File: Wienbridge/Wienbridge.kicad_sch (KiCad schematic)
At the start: 23 parts, among them J1 OUTPUT, U1 OP07, U2 OP07, U3 OP07

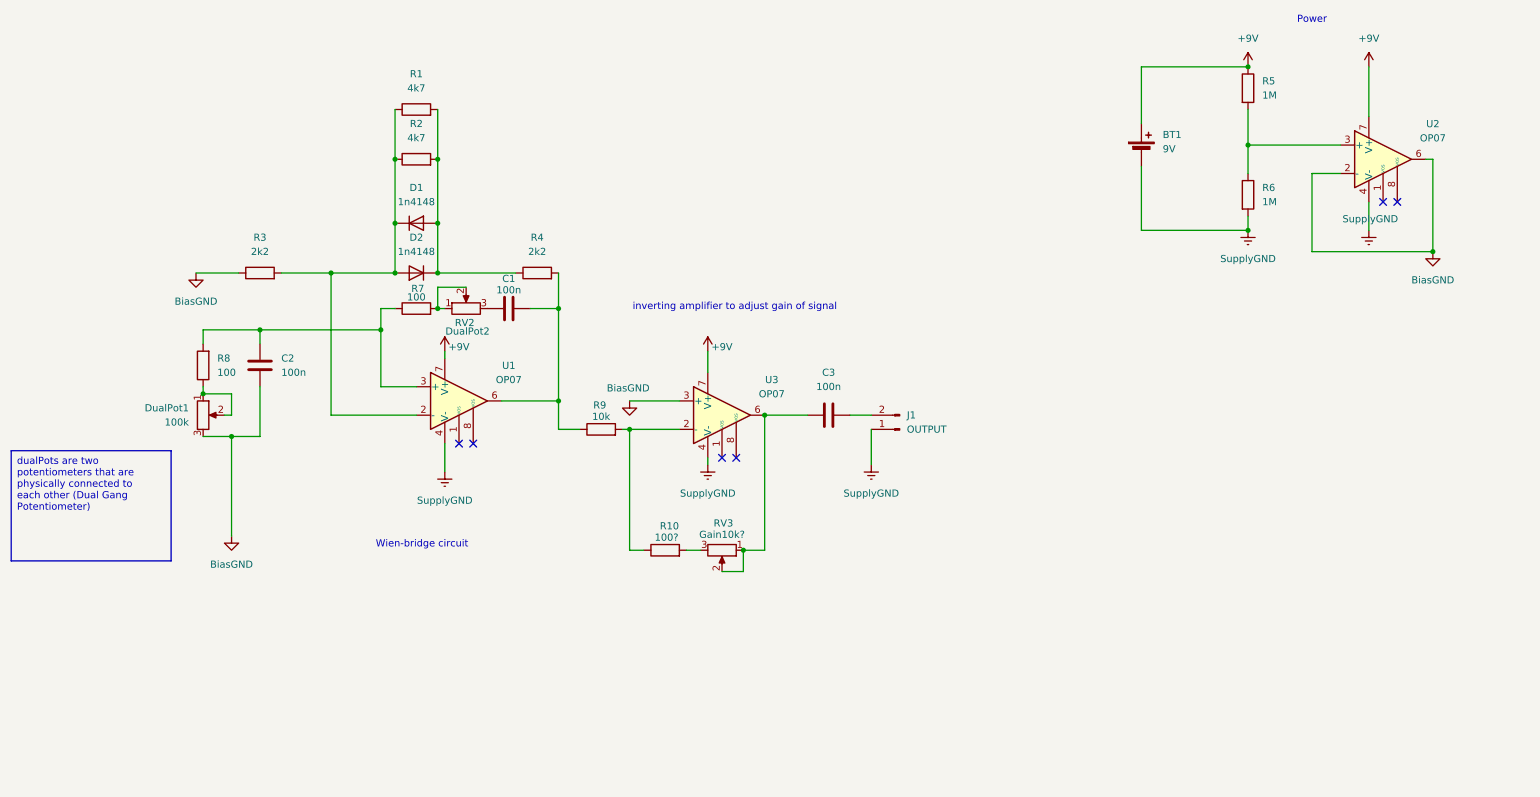
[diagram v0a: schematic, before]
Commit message: finished first revision of the pcb of wien-bridge
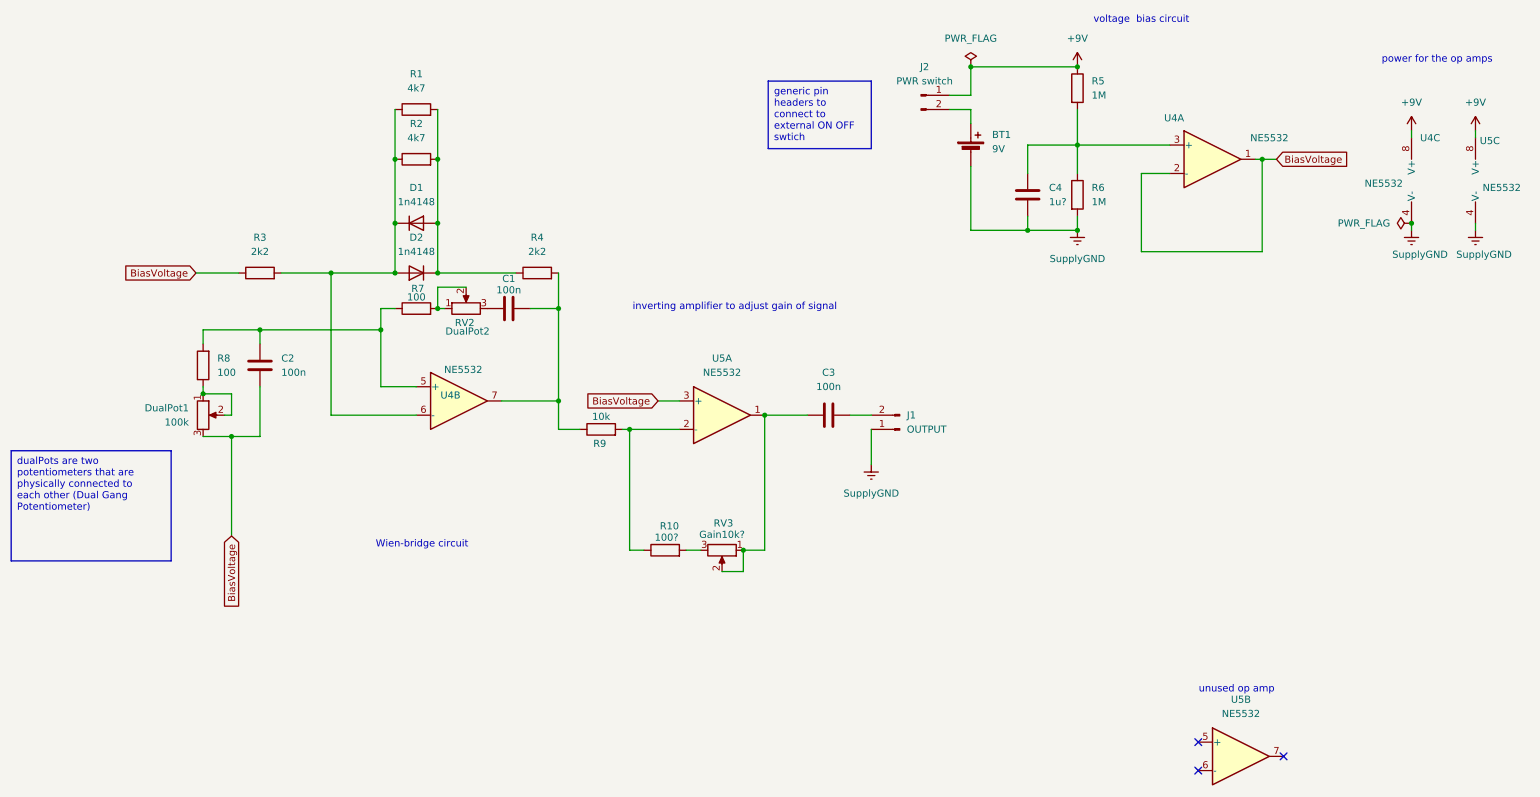
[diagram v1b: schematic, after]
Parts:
- removed U1, U2, U3: OP07, symbol Amplifier_Operational:OP07
- added C4: 1u?, Capacitor_SMD:C_0603_1608Metric_Pad1.08x0.95mm_HandSolder, symbol Device:C
- added J2: PWR switch, Connector_PinHeader_2.54mm:PinHeader_1x02_P2.54mm_Vertical, symbol Connector:Conn_01x02_Pin
- added U4, U5: NE5532, Package_DIP:DIP-8_W7.62mm, symbol Amplifier_Operational:NE5532
- R10: footprint (none) -> Resistor_SMD:R_0603_1608Metric_Pad0.98x0.95mm_HandSolder
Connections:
- net +9V: now also J2.1 (Pin_1), U4.8 (V+), U5.8 (V+); no longer BT1.1 (+)
- net SupplyGND: now also C4.2, U4.4 (V-), U5.4 (V-)
- net at D1.1 (K), D2.2 (A), R1.1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: now also U4.6 (-)
- net at C1.2, R4.2, R9.1: now also U4.7
- net at R10.1, R9.2: now also U5.2 (-)
- net at C2.1, R7.1, R8.2: now also U4.5 (+)
- net at C3.1, RV3.1, RV3.2: now also U5.1
- net at R5.2, R6.1: now also C4.1, U4.3 (+)
- net BiasGND renamed BiasVoltage
- net BiasVoltage: now also U4.1, U4.2 (-), U5.3 (+)
- new net: BT1.1 (+), J2.2 (Pin_2)
- no-connect marks 6 -> 3
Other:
- note added: "power for the op amps"
- note added: "unused op amp"
- note added: "voltage bias circuit"
- note removed: "Power"
- moved on the sheet: BT1, R5, R6

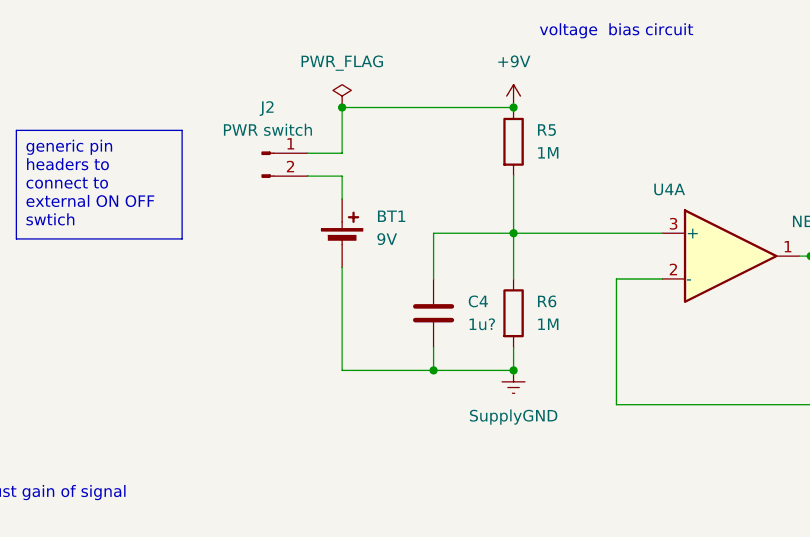
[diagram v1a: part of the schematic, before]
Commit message: few additions to the wein-brdige circuit and finished first revision of the opamp distortion schematic
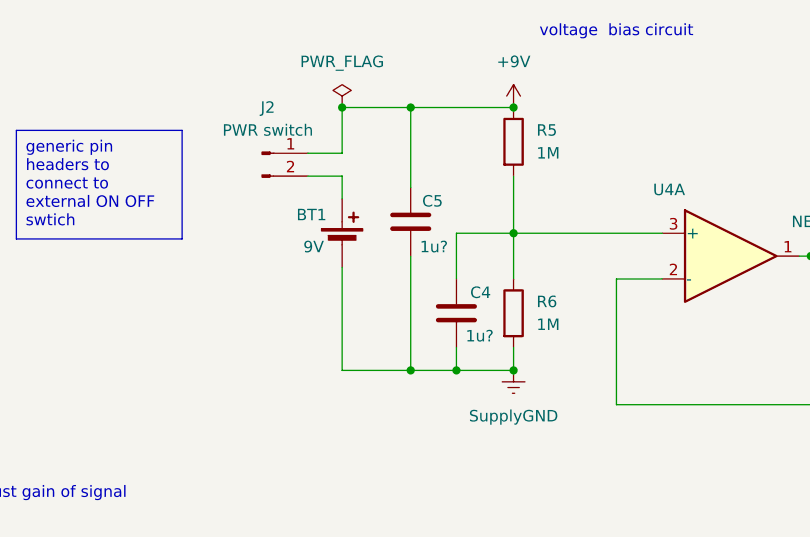
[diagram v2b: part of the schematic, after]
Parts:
- added C5: 1u?, Capacitor_SMD:C_0603_1608Metric_Pad1.08x0.95mm_HandSolder, symbol Device:C
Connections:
- net +9V: now also C5.1
- net SupplyGND: now also C5.2
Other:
- moved on the sheet: C4
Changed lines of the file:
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@@
 	)
 	(junction
+		(at 196.85 54.61)
+		(diameter 0)
+		(color 0 0 0 0)
+	)
+	(junction
 		(at 110.49 68.58)
 		(diameter 0)
@@
 	)
 	(junction
+		(at 191.77 25.4)
+		(diameter 0)
+		(color 0 0 0 0)
+	)
+	(junction
+		(at 191.77 54.61)
+		(diameter 0)
+		(color 0 0 0 0)
+	)
+	(junction
 		(at 81.28 41.91)
 		(diameter 0)
@@
 	)
 	(junction
-		(at 194.31 54.61)
-		(diameter 0)
-		(color 0 0 0 0)
-	)
-	(junction
 		(at 46.99 83.82)
 		(diameter 0)
@@
 	(wire
 		(pts
-			(xy 194.31 52.07) (xy 194.31 54.61)
+			(xy 196.85 52.07) (xy 196.85 54.61)
 		)
 		(stroke
@@
 	(wire
 		(pts
-			(xy 194.31 54.61) (xy 203.2 54.61)
-		)
-		(stroke
-			(width 0)
-			(type default)
-		)
-	)
-	(wire
-		(pts
 			(xy 214.63 58.42) (xy 236.22 58.42)
 		)
@@
 	(wire
 		(pts
-			(xy 194.31 39.37) (xy 203.2 39.37)
+			(xy 196.85 39.37) (xy 203.2 39.37)
 		)
 		(stroke
@@
 	(wire
 		(pts
+			(xy 196.85 54.61) (xy 203.2 54.61)
+		)
+		(stroke
+			(width 0)
+			(type default)
+		)
+	)
+	(wire
+		(pts
 			(xy 128.27 85.09) (xy 132.08 85.09)
 		)
@@
 	(wire
 		(pts
+			(xy 191.77 25.4) (xy 191.77 34.29)
+		)
+		(stroke
+			(width 0)
+			(type default)
+		)
+	)
+	(wire
+		(pts
 			(xy 147.32 87.63) (xy 154.94 87.63)
 		)
@@
 	(wire
 		(pts
+			(xy 191.77 54.61) (xy 196.85 54.61)
+		)
+		(stroke
+			(width 0)
+			(type default)
+		)
+	)
+	(wire
+		(pts
 			(xy 45.72 62.23) (xy 53.34 62.23)
 		)
@@
 	(wire
 		(pts
+			(xy 191.77 25.4) (xy 203.2 25.4)
+		)
+		(stroke
+			(width 0)
+			(type default)
+		)
+	)
+	(wire
+		(pts
 			(xy 139.7 115.57) (xy 143.51 115.57)
 		)
@@
 	(wire
 		(pts
-			(xy 184.15 25.4) (xy 203.2 25.4)
+			(xy 184.15 25.4) (xy 191.77 25.4)
 		)
 		(stroke
@@
 	(wire
 		(pts
-			(xy 184.15 54.61) (xy 194.31 54.61)
+			(xy 184.15 54.61) (xy 191.77 54.61)
 		)
 		(stroke
@@
 	(wire
 		(pts
-			(xy 194.31 44.45) (xy 194.31 39.37)
+			(xy 196.85 44.45) (xy 196.85 39.37)
 		)
 		(stroke
@@
 	(wire
 		(pts
+			(xy 191.77 41.91) (xy 191.77 54.61)
+		)
+		(stroke
+			(width 0)
+			(type default)
+		)
+	)
+	(wire
+		(pts
 			(xy 88.9 62.23) (xy 102.87 62.23)
 		)
@@
 		(on_board yes)
 		(dnp no)
-		(fields_autoplaced yes)
 		(property "Reference" "BT1"
-			(at 187.96 37.5284 0)
+			(at 179.07 37.338 0)
 			(effects
 				(font
@@
 		)
 		(property "Value" "9V"
-			(at 187.96 40.0684 0)
+			(at 179.832 40.894 0)
 			(effects
 				(font
@@
 	)
 	(symbol
+		(lib_id "Device:C")
+		(at 191.77 38.1 0)
+		(unit 1)
+		(exclude_from_sim no)
+		(in_bom yes)
+		(on_board yes)
+		(dnp no)
+		(property "Reference" "C5"
+			(at 193.04 35.814 0)
+			(effects
+				(font
+					(size 1.27 1.27)
+				)
+				(justify left)
+			)
+		)
+		(property "Value" "1u?"
+			(at 192.786 40.894 0)
+			(effects
+				(font
+					(size 1.27 1.27)
+				)
+				(justify left)
+			)
+		)
+		(property "Footprint" "Capacitor_SMD:C_0603_1608Metric_Pad1.08x0.95mm_HandSolder"
+			(at 192.7352 41.91 0)
+			(effects
+				(font
+					(size 1.27 1.27)
+				)
+				(hide yes)
+			)
+		)
+		(property "Datasheet" "~"
+			(at 191.77 38.1 0)
+			(effects
+				(font
+					(size 1.27 1.27)
+				)
+				(hide yes)
+			)
+		)
+		(property "Description" "Unpolarized capacitor"
+			(at 191.77 38.1 0)
+			(effects
+				(font
+					(size 1.27 1.27)
+				)
+				(hide yes)
+			)
+		)
+		(pin "2"
+		)
+		(pin "1"
+		)
+		(instances
+			(project ""
+				(path "/15d9c779-f062-42d2-9e52-f5c6a501706f"
+					(reference "C5")
+					(unit 1)
+				)
+			)
+		)
+	)
+	(symbol
 		(lib_id "Amplifier_Operational:NE5532")
 		(at 232.41 148.59 0)
@@
 	(symbol
 		(lib_id "Device:C")
-		(at 194.31 48.26 0)
+		(at 196.85 48.26 0)
 		(unit 1)
 		(exclude_from_sim no)
@@
 		(on_board yes)
 		(dnp no)
-		(fields_autoplaced yes)
 		(property "Reference" "C4"
-			(at 198.12 46.9899 0)
+			(at 198.374 45.974 0)
 			(effects
 				(font
@@
 		)
 		(property "Value" "1u?"
-			(at 198.12 49.5299 0)
+			(at 197.866 50.8 0)
 			(effects
 				(font
@@
 		)
 		(property "Footprint" "Capacitor_SMD:C_0603_1608Metric_Pad1.08x0.95mm_HandSolder"
-			(at 195.2752 52.07 0)
+			(at 197.8152 52.07 0)
 			(effects
 				(font
@@
 		)
 		(property "Datasheet" "~"
-			(at 194.31 48.26 0)
+			(at 196.85 48.26 0)
 			(effects
 				(font
@@
 		)
 		(property "Description" "Unpolarized capacitor"
-			(at 194.31 48.26 0)
+			(at 196.85 48.26 0)
 			(effects
 				(font
